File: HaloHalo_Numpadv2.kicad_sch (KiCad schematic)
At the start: 92 parts, among them SW1 SW_SPST, SW10 SW_SPST, SW11 SW_SPST, SW12 SW_SPST, SW13 SW_SPST, SW14 SW_SPST, SW15 SW_SPST, SW16 SW_SPST, SW17 SW_SPST, SW18 SW_SPST, SW19 SW_SPST, SW2 SW_SPST, SW20 SW_SPST, SW21 RotaryEncoder_Switch, SW22 RotaryEncoder_Switch, SW23 RotaryEncoder_Switch, SW3 SW_SPST, SW4 SW_SPST, SW5 SW_SPST, SW6 SW_SPST, SW7 SW_SPST, SW8 SW_SPST, SW9 SW_SPST

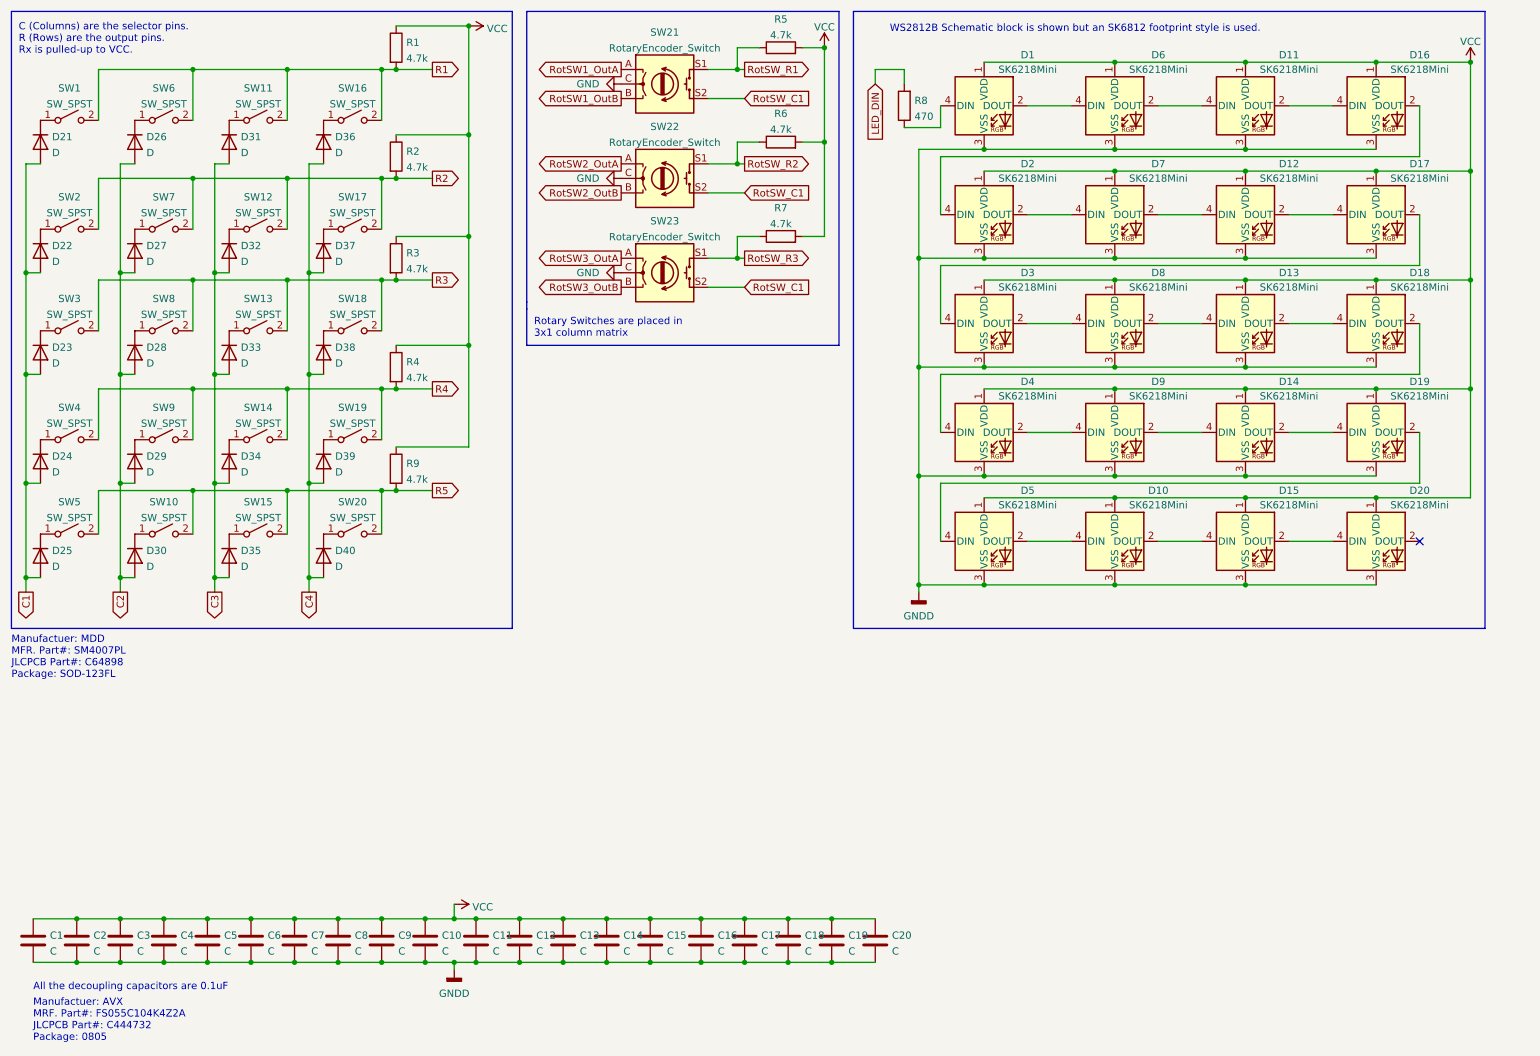
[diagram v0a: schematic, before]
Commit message: Updated schematic fields. Uploaded PDFs and images of schematic.
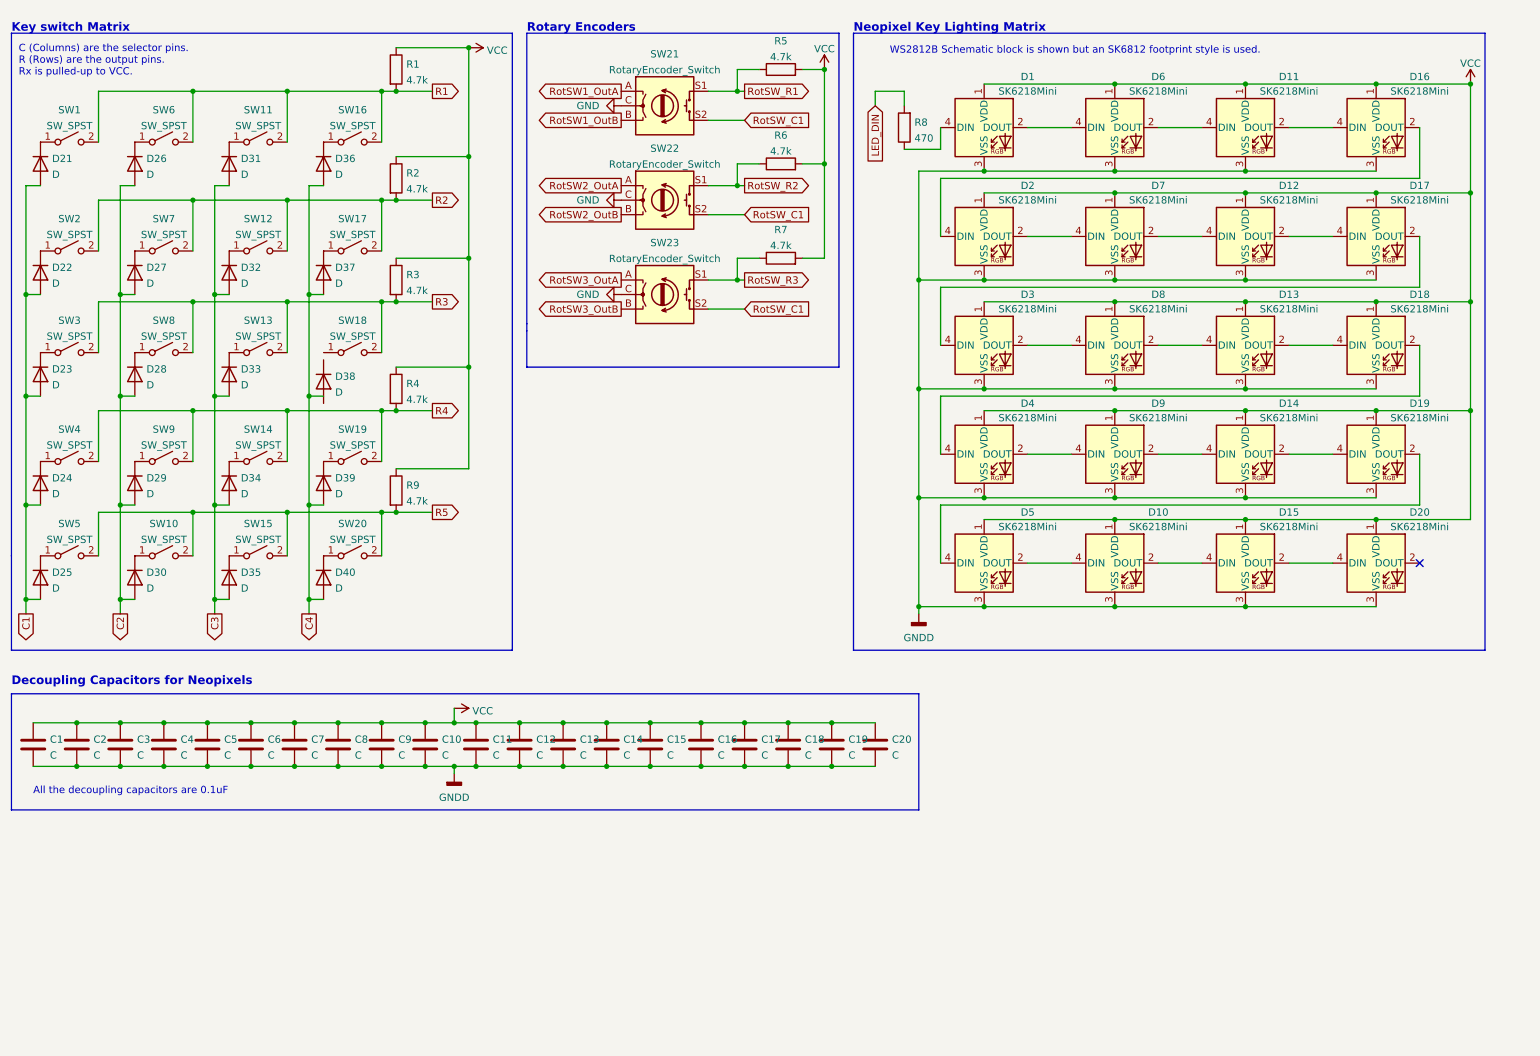
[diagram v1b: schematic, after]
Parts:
- C1: LCSC Part Number (none) -> C444732; MFR. Part Number (none) -> FS055C104K4Z2A; Manufacturer (none) -> AVX
- D21, D22, D23, D24, D25, D26, D27, D28, D29, D30, D31, D32, D33, D34, D35, D36, D37, D38, D39, D40: LCSC Part Number (none) -> C64898; MFR. Part Number (none) -> SM4007PL; Manufacturer (none) -> MDD
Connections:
- net C4: no longer D38.2 (A)
- net at SW18.1 (A): no longer D38.1 (K)
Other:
- note added: "Decoupling Capacitors for Neopixels"
- note added: "Key switch Matrix"
- note added: "Neopixel Key Lighting Matrix"
- note added: "Rotary Encoders"
- note removed: "Manufactuer: AVX MRF. Part#: FS055C104K4Z2A JLCPCB Part#: C444732 Package: 0805"
- note removed: "Manufactuer: MDD MFR. Part#: SM4007PL JLCPCB Part#: C64898 Package: SOD-123FL"
- note removed: "Rotary Switches are placed in 3x1 column matrix"
- moved on the sheet: C1, C10, C11, C12, C13, C14, C15, C16, C17, C18, C19, C2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

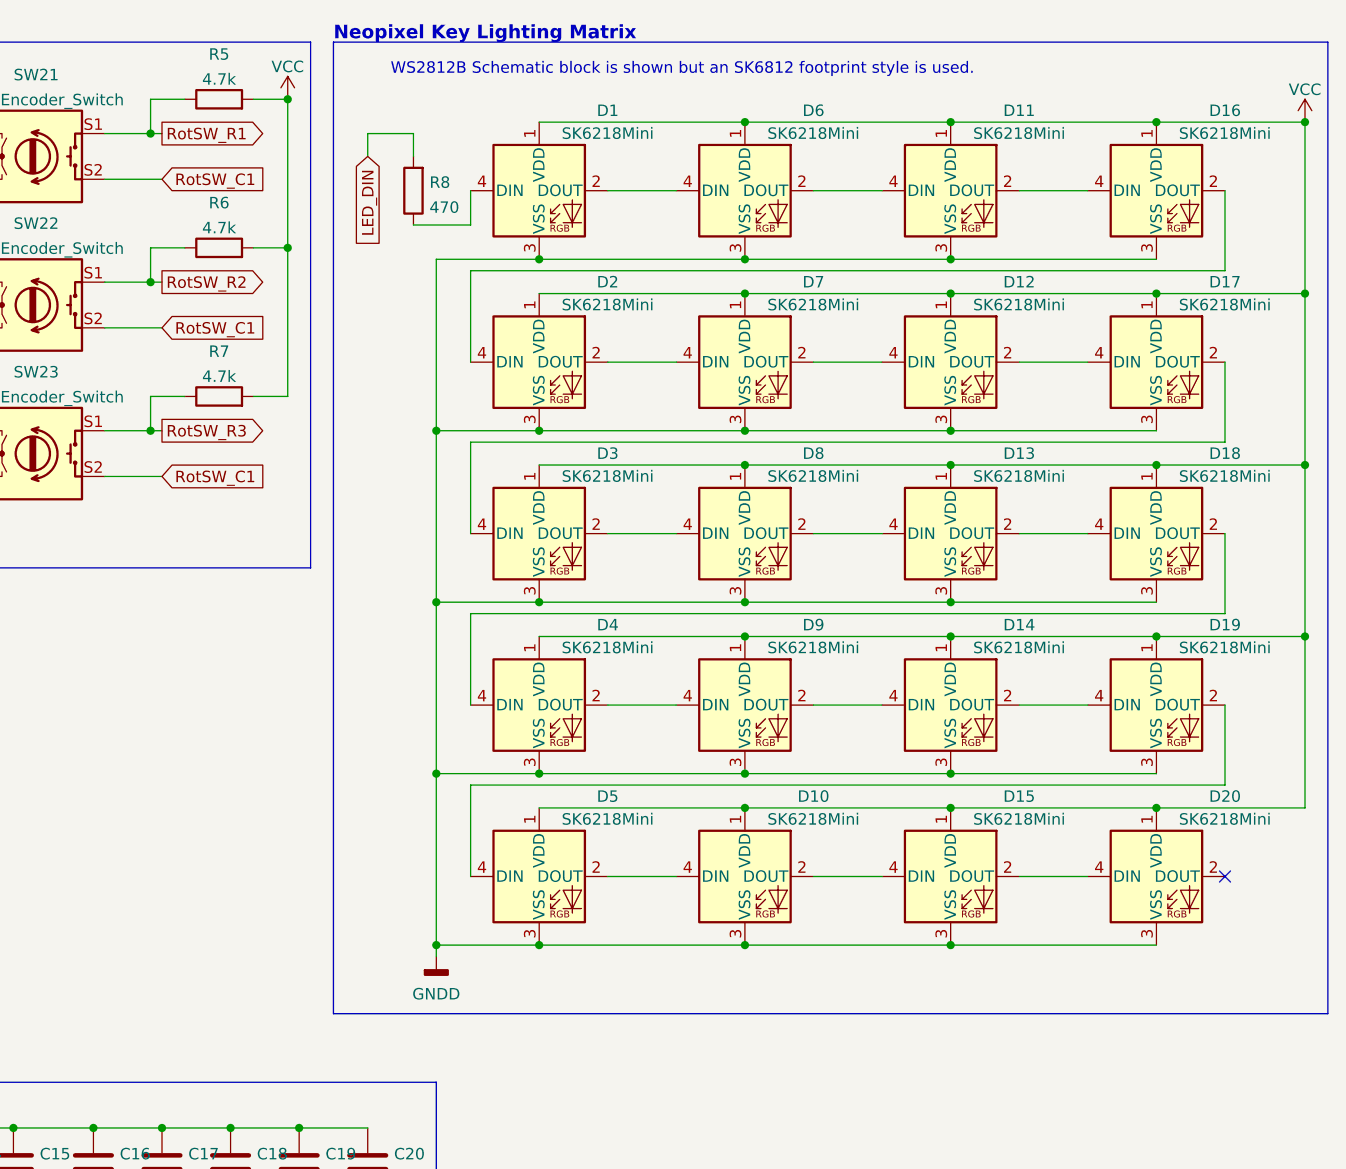
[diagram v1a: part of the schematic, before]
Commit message: Start ignorning SVGs and updated PDF and PNG of Numpad Schematic
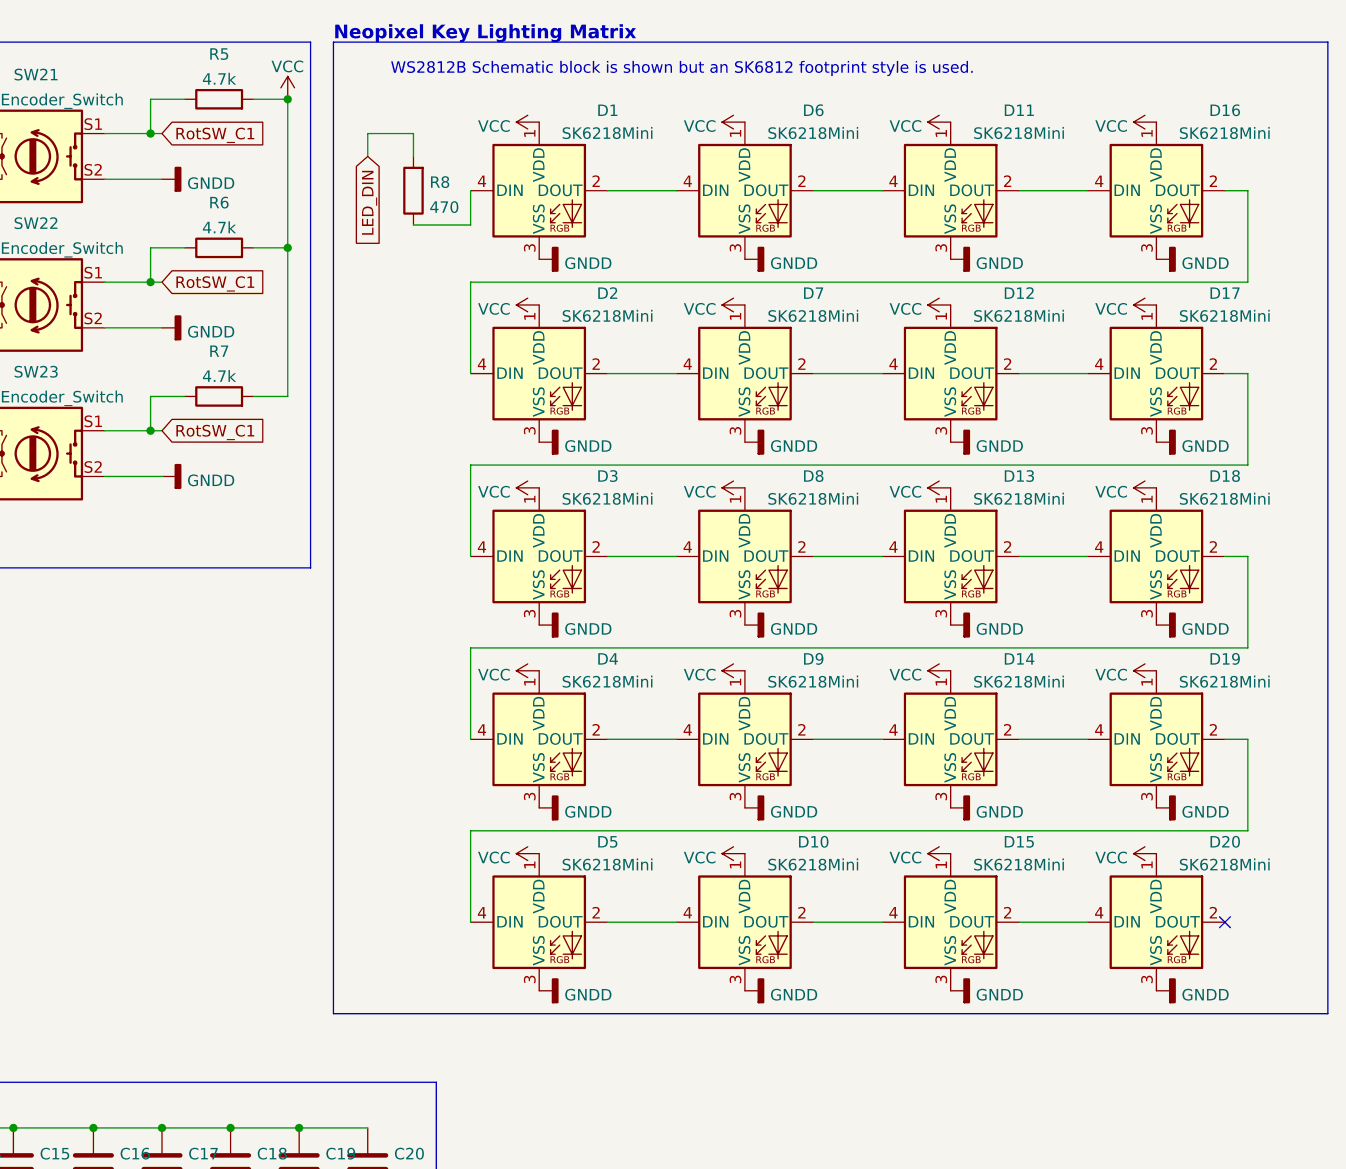
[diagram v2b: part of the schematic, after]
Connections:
- net RotSW_R1 is gone; now on net RotSW_C1: R5.1, SW21.S1
- net RotSW_R2 is gone; now on net RotSW_C1: R6.1, SW22.S1
- net RotSW_R3 is gone; now on net RotSW_C1: R7.1, SW23.S1
- net GNDD: now also SW21.S2, SW22.S2, SW23.S2
- net RotSW_C1: no longer SW21.S2, SW22.S2, SW23.S2
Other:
- moved on the sheet: D10, D12, D13, D14, D15, D17, D18, D19, D2, D20, D3, D4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

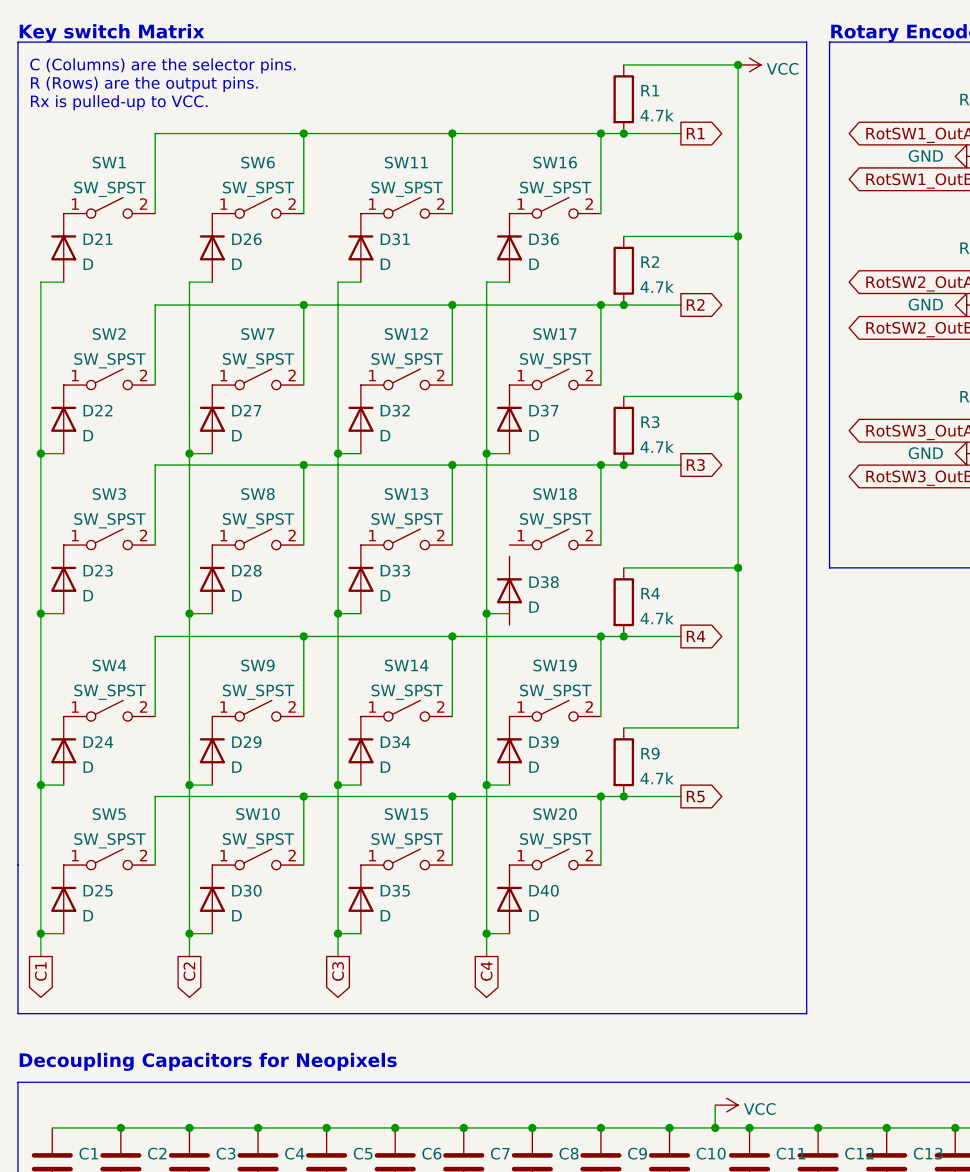
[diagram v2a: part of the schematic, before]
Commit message: Fixed wiring of active low switch matrix in Eschema. Updated corresponding PNG and PDF file for schematic.
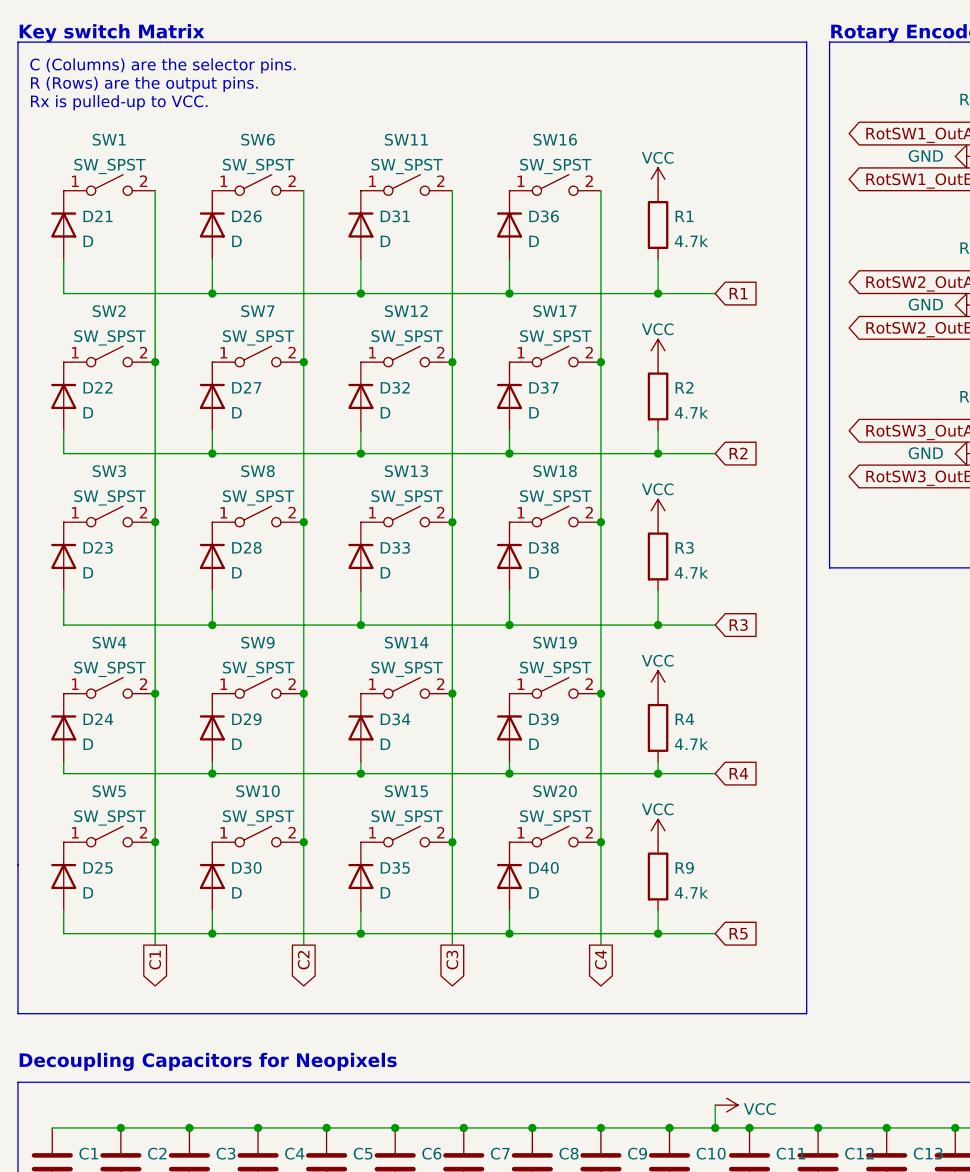
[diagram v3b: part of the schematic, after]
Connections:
- net C1: now also SW1.2 (B), SW2.2 (B), SW3.2 (B), SW4.2 (B), SW5.2 (B); no longer D21.2 (A), D22.2 (A), D23.2 (A), D24.2 (A), D25.2 (A)
- net C2: now also SW10.2 (B), SW6.2 (B), SW7.2 (B), SW8.2 (B), SW9.2 (B); no longer D26.2 (A), D27.2 (A), D28.2 (A), D29.2 (A), D30.2 (A)
- net C3: now also SW11.2 (B), SW12.2 (B), SW13.2 (B), SW14.2 (B), SW15.2 (B); no longer D31.2 (A), D32.2 (A), D33.2 (A), D34.2 (A), D35.2 (A)
- net C4: now also SW16.2 (B), SW17.2 (B), SW18.2 (B), SW19.2 (B), SW20.2 (B); no longer D36.2 (A), D37.2 (A), D39.2 (A), D40.2 (A)
- net R1: now also D21.2 (A), D26.2 (A), D31.2 (A), D36.2 (A); no longer SW1.2 (B), SW11.2 (B), SW16.2 (B), SW6.2 (B)
- net R2: now also D22.2 (A), D27.2 (A), D32.2 (A), D37.2 (A); no longer SW12.2 (B), SW17.2 (B), SW2.2 (B), SW7.2 (B)
- net R3: now also D23.2 (A), D28.2 (A), D33.2 (A), D38.2 (A); no longer SW13.2 (B), SW18.2 (B), SW3.2 (B), SW8.2 (B)
- net R4: now also D24.2 (A), D29.2 (A), D34.2 (A), D39.2 (A); no longer SW14.2 (B), SW19.2 (B), SW4.2 (B), SW9.2 (B)
- net R5: now also D25.2 (A), D30.2 (A), D35.2 (A), D40.2 (A); no longer SW10.2 (B), SW15.2 (B), SW20.2 (B), SW5.2 (B)
- net at SW18.1 (A): now also D38.1 (K)
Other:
- moved on the sheet: D21, D22, D23, D24, D25, D26, D27, D28, D29, D30, D31, D32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
